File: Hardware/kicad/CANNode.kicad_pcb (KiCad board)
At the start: 4 copper layers, 66 x 57.5 mm, 53 parts, among them J1 Conn_01x04, J11 Conn_01x04, J12 Conn_01x04, J2 Conn_01x04, J21 Conn_01x04, J31 Conn_01x04, J41 Conn_01x04, J42 Conn_01x04, J43 Conn_01x04, J44 Conn_01x04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

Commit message: almost routed
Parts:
- moved J51 17.5 mm to (113.4, 65.5)
- moved JP22 2.03 mm to (116.5, 65.5)
- moved R6 1.85 mm to (79.4, 45.7)
- moved JP21 0.51 mm to (119.0, 65.5)
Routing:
- net +12V: track 10.7 -> 128.2 mm, vias 0 -> 9
- net +3V3: track 19.4 -> 107.5 mm, vias 1 -> 3
- net /6: track 0.00 -> 21.2 mm
- net Net-(J12-Pad2): track 2.64 -> 23.1 mm
- net /10: track 0.00 -> 20.1 mm, vias 0 -> 1
- net /OW14: track 2.64 -> 19.6 mm
- net Net-(J61-Pad7): track 21.5 -> 5.71 mm
- net Net-(JP22-Pad1): track 16.3 -> 3.60 mm
- net /EN34_9: track 23.6 -> 11.7 mm
- net Net-(J31-Pad4): track 0.00 -> 10.1 mm
- net /SCL0_16: track 24.0 -> 14.7 mm
- net Net-(JP21-Pad1): track 10.0 -> 1.94 mm
- net Net-(J41-Pad4): track 0.00 -> 7.62 mm
- net +5V: track 41.0 -> 46.3 mm, vias 0 -> 8
- net /UA1-: track 15.2 -> 19.8 mm
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- added copper zone on In2.Cu, net +12V
- added copper zone on In2.Cu, net +5V

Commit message: looks good
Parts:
- removed J51: Conn_01x02, Connector_PinHeader_2.54mm:PinHeader_1x02_P2.54mm_Vertical
- removed JP22: Jumper_NC_Small, Connector_PinHeader_2.54mm:PinHeader_1x02_P2.54mm_Vertical
- removed the REF** at (72.8, 91.7)
- removed the REF** at (109.3, 54.7)
- removed the REF** at (99.9, 77.2)
- removed the REF** at (72.8, 39.2)
- added ?: , own:LOGO_MID, F.Cu at (71.0, 64.3)
- added ?: , own:LOGO_MID, B.Cu at (88.5, 63.0)
- added REF**: MountingHole_2.5mm, MountingHole:MountingHole_2.5mm, F.Cu at (109.3, 54.2)
- added REF**: MountingHole_2.5mm, MountingHole:MountingHole_2.5mm, F.Cu at (71.8, 91.2)
- added REF**: MountingHole_2.5mm, MountingHole:MountingHole_2.5mm, F.Cu at (71.8, 39.2)
- added REF**: MountingHole_2.5mm, MountingHole:MountingHole_2.5mm, F.Cu at (133.3, 39.2)
- added REF**: MountingHole_2.5mm, MountingHole:MountingHole_2.5mm, F.Cu at (133.3, 91.2)
- added REF**: KiCAD Logo, Symbol:Symbol_KiCAD-Logo_CopperAndSilkScreenTop, F.Cu at (72.3, 76.2)
- added REF**: OSHW-Symbol_6.7x6mm_SilkScreen, Symbol:OSHW-Symbol_6.7x6mm_SilkScreen, F.Cu at (72.8, 59.4)
- JP21: value Jumper_NC_Small -> Conn_02x03_Odd_Even; footprint Connector_PinHeader_2.54mm:PinHeader_1x02_P2.54mm_Vertical -> Connector_PinHeader_2.54mm:PinHeader_2x03_P2.54mm_Vertical
- moved JP21 3.06 mm to (118.7, 62.5), turned to 270 degrees
- moved J61 0.80 mm to (121.3, 72.4)
- moved J91 0.63 mm to (128.9, 78.1)
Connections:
- J61 pad 7: Net-(J61-Pad7) -> /SDA0_17
- JP21 pad 1: Net-(JP21-Pad1) -> /SCL0_16
- JP21 pad 2: /SCL0_16 -> Net-(JP21-Pad2)
- R21 pad 1: Net-(JP21-Pad1) -> Net-(JP21-Pad2)
- R22 pad 1: Net-(JP22-Pad1) -> Net-(JP21-Pad4)
- U1 pad 19: Net-(J51-Pad2) -> Net-(JP21-Pad5)
- U1 pad 24: Net-(J61-Pad7) -> /SDA0_17
- U21 pad 3: Net-(JP21-Pad1) -> Net-(JP21-Pad2)
- U21 pad 4: Net-(JP22-Pad1) -> Net-(JP21-Pad4)
- U41 pad 15: Net-(J61-Pad7) -> /SDA0_17
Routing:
- net /SDA0_17: track 0.00 -> 33.1 mm
- net Net-(J61-Pad8): track 0.00 -> 22.7 mm, vias 0 -> 1
- net /SCL0_16: track 14.7 -> 35.8 mm
- net Net-(JP21-Pad4): track 0.00 -> 17.1 mm
- net /EN34_9: track 11.7 -> 26.0 mm
- net Net-(J61-Pad4): track 0.00 -> 13.3 mm
- net +3V3: track 107.5 -> 118.5 mm, vias 3 -> 5
- net +12V: track 128.2 -> 117.4 mm
- net Net-(JP21-Pad2): track 0.00 -> 10.4 mm
- net /CAN+: track 48.2 -> 58.3 mm
- net /CAN-: track 42.6 -> 52.8 mm
- net Net-(J61-Pad6): track 0.00 -> 7.85 mm
- net Net-(J61-Pad7): track 5.71 -> 0.00 mm
- net Net-(JP21-Pad5): track 0.00 -> 4.44 mm
- net Net-(JP22-Pad1): track 3.60 -> 0.00 mm
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- added copper zone on F.Cu, net (none)
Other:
- board size 66 x 57.5 mm -> 66.5 x 57 mm
- board text added: "+"
- board text added: "-"
- board text added: "10"
- board text added: "12V"
- board text added: "16"
- board text added: "17"
- board text added: "20"
- board text added: "21"
- board text added: "22"
- board text added: "23"
- board text added: "3V3"
- board text added: "5V"
- board text added: "6"
- board text added: "<- TERM"
- board text added: "CAN"
- board text added: "D+"
- board text added: "D-"
- board text added: "DAC"
- board text added: "DIfferential OUT"
- board text added: "GND"
- board text added: "MISO"
- board text added: "MOSI"
- board text added: "One Wire"
- board text added: "P14"
- board text added: "P15"
- board text added: "PWR"
- board text added: "RS485 DMX"
- board text added: "Rev. 2.0"
- board text added: "SCL"
- board text added: "SDA"
- board text added: "wiebel.org/CANNode"

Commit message: late changes
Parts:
- added C1: CP, Capacitor_SMD:CP_Elec_3x5.4, B.Cu at (104.1, 83.8)
- added C2: CP, Capacitor_SMD:CP_Elec_3x5.4, B.Cu at (118.1, 83.8)

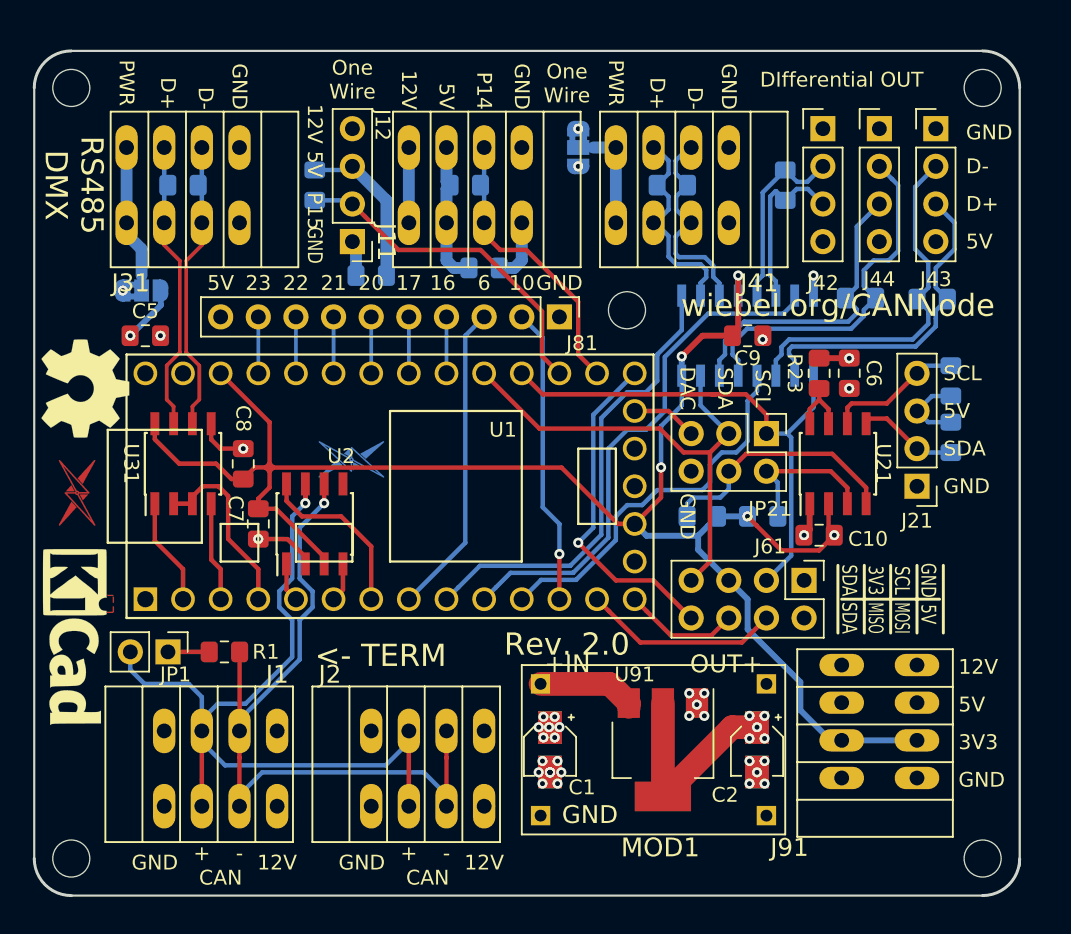
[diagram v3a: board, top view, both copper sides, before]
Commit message: more clearance in Layer 2
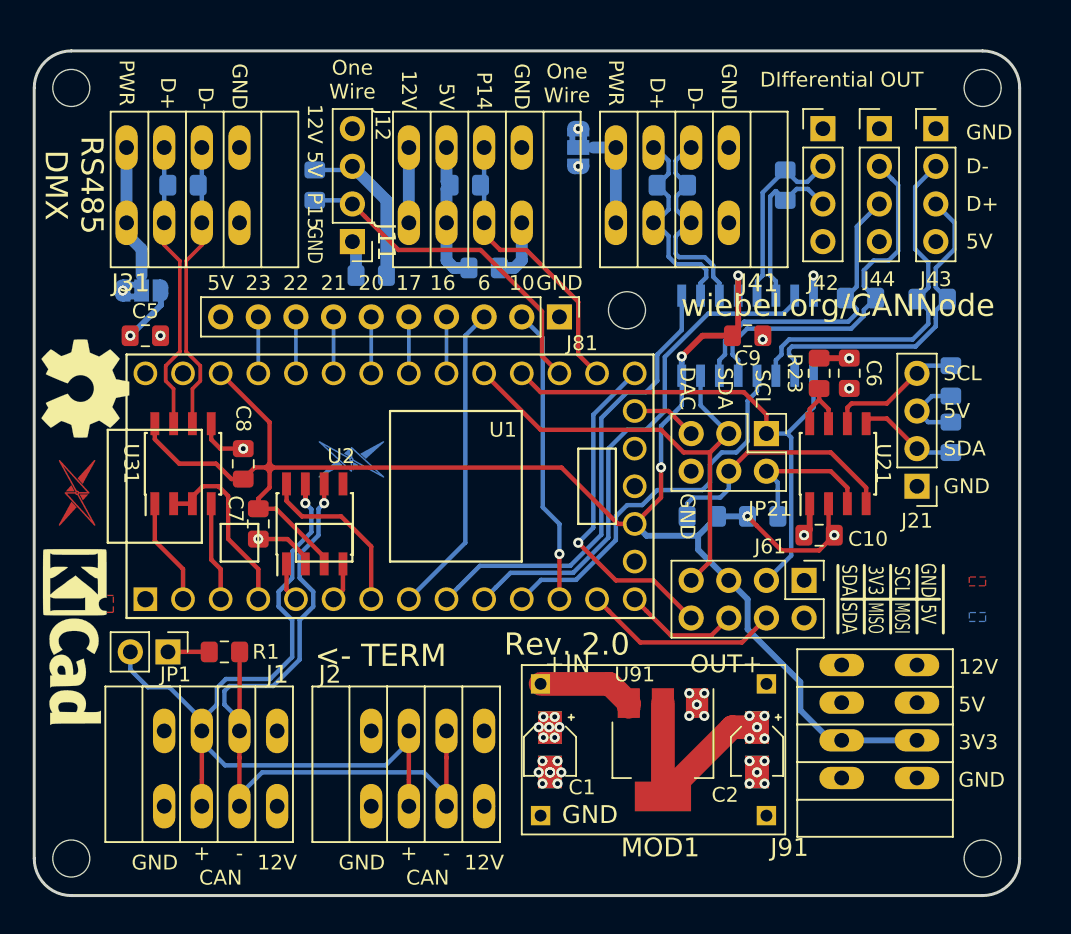
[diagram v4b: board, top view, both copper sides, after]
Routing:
- net +12V: track 117.4 -> 134.0 mm
- net /CAN-: track 52.8 -> 55.4 mm
- added copper zone on B.Cu, net (none)
- added copper zone on In1.Cu, net (none)
- added copper zone on In2.Cu, net (none)
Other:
- outline, holes or cut-outs redrawn

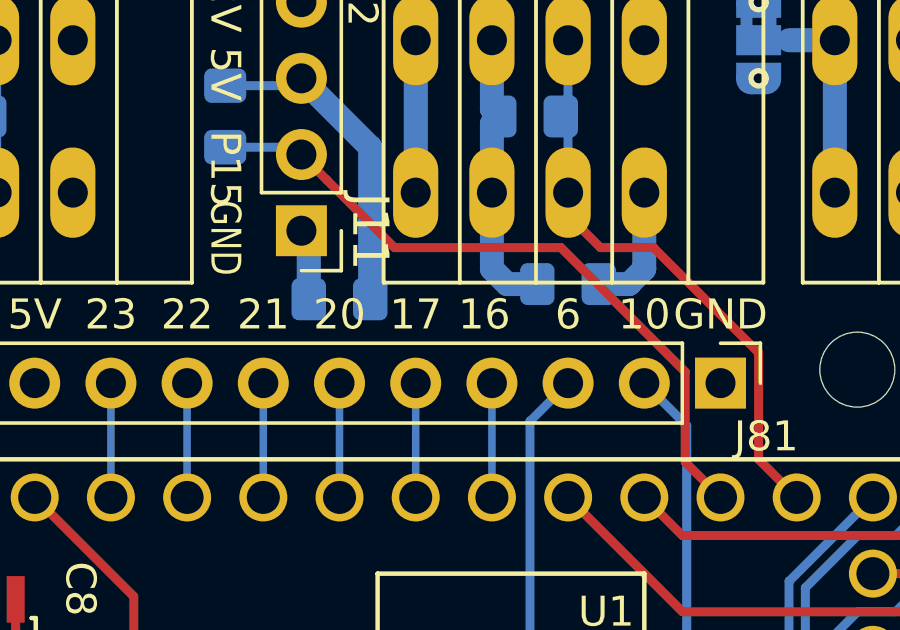
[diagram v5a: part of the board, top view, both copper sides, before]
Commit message: corrected  output port labels
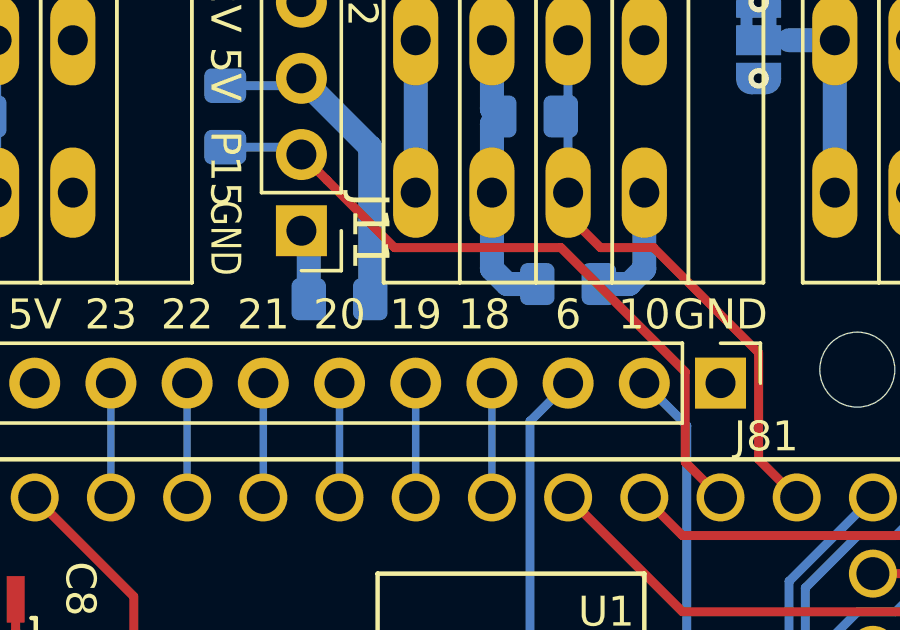
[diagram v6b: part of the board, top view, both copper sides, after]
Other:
- board text added: "18"
- board text added: "19"
- board text removed: "16"
- board text removed: "17"
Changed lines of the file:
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@@
     (35 F.Paste user hide)
     (36 B.SilkS user hide)
-    (37 F.SilkS user hide)
+    (37 F.SilkS user)
     (38 B.Mask user)
     (39 F.Mask user)
@@
     (effects (font (size 1 1) (thickness 0.25)))
   )
-  (gr_text 16 (at 96.901 52.324) (layer F.SilkS)
+  (gr_text 18 (at 96.901 52.324) (layer F.SilkS)
     (effects (font (size 1 1) (thickness 0.25)))
   )
-  (gr_text 17 (at 94.615 52.324) (layer F.SilkS)
+  (gr_text 19 (at 94.615 52.324) (layer F.SilkS)
     (effects (font (size 1 1) (thickness 0.25)))
   )

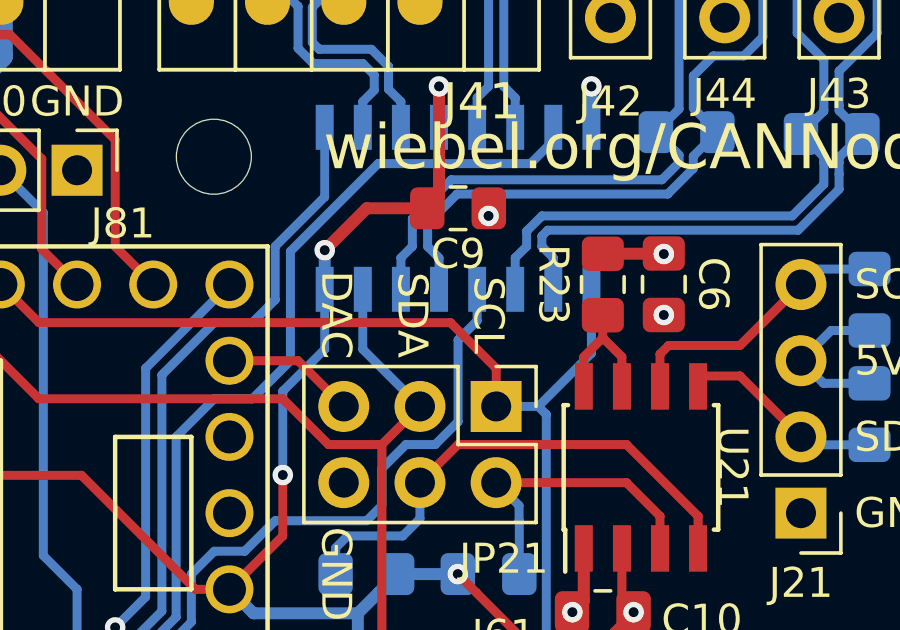
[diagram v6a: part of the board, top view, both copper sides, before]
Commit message: ena I²C text
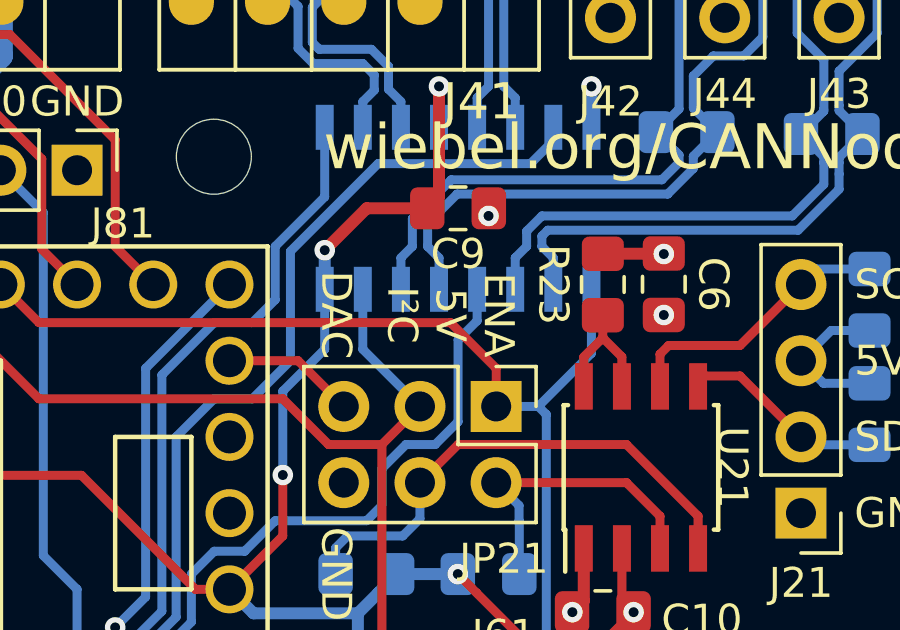
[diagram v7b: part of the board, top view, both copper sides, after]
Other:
- board text added: "ENA 5V I²C"
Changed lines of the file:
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@@
   (general
     (thickness 1.6)
-    (drawings 87)
+    (drawings 86)
     (tracks 549)
     (zones 0)
@@
     (effects (font (size 1 1) (thickness 0.25)))
   )
-  (gr_text SCL (at 118.491 59.436 270) (layer F.SilkS)
-    (effects (font (size 1 1) (thickness 0.25)))
-  )
-  (gr_text SDA (at 115.951 59.436 270) (layer F.SilkS)
+  (gr_text "ENA\n5V\nI²C" (at 117.221 59.436 270) (layer F.SilkS)
     (effects (font (size 1 1) (thickness 0.25)))
   )
